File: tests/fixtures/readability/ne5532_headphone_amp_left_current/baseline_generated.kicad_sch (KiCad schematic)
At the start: 13 parts, among them J1 AudioIn_L, J2 AudioIn_R, J3 PowerSupply, J4 HeadphoneOut_L, J5 HeadphoneOut_R

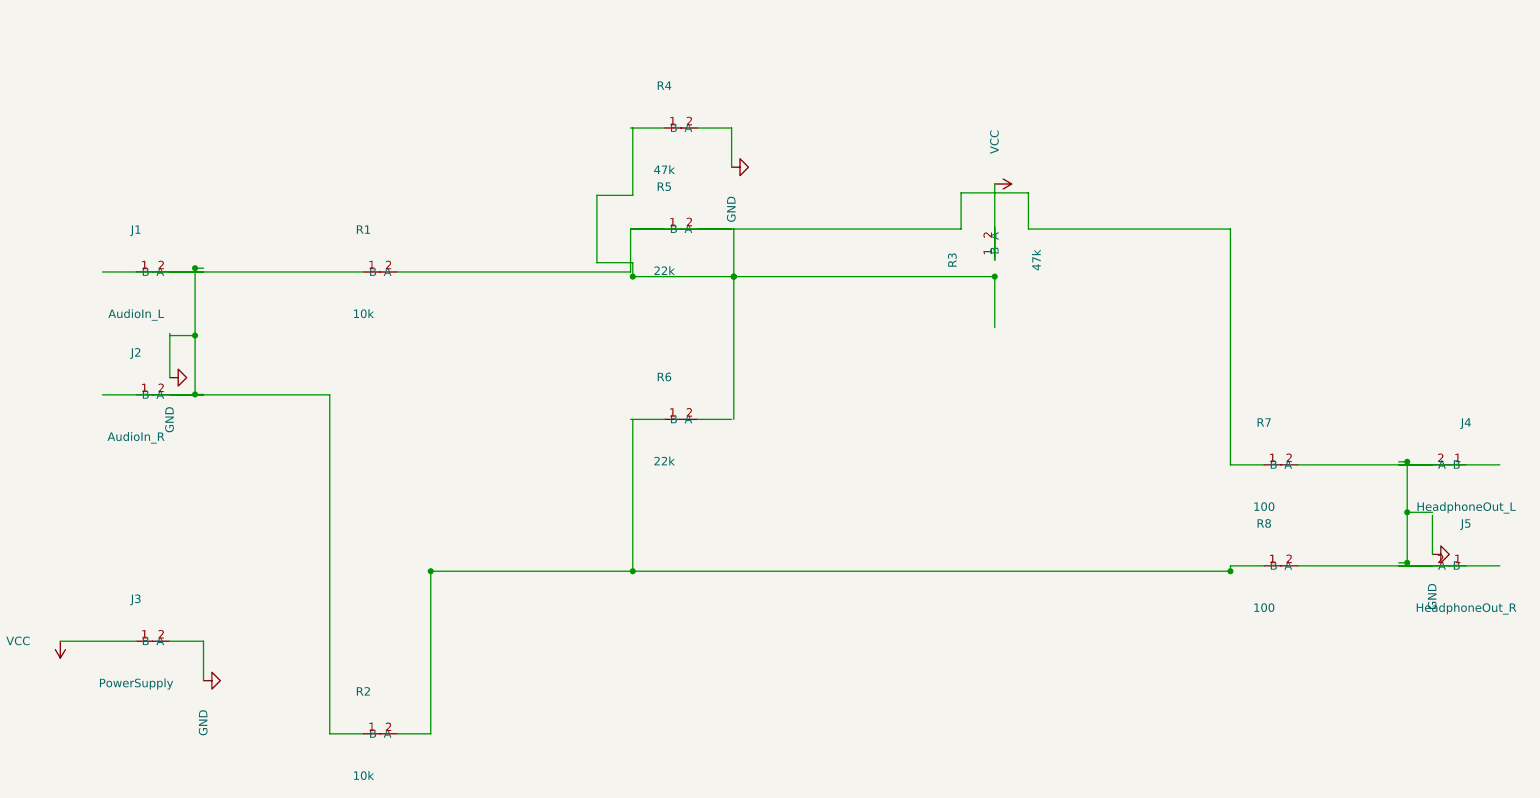
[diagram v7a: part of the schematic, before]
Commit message: feat: improve multi-unit schematic generation
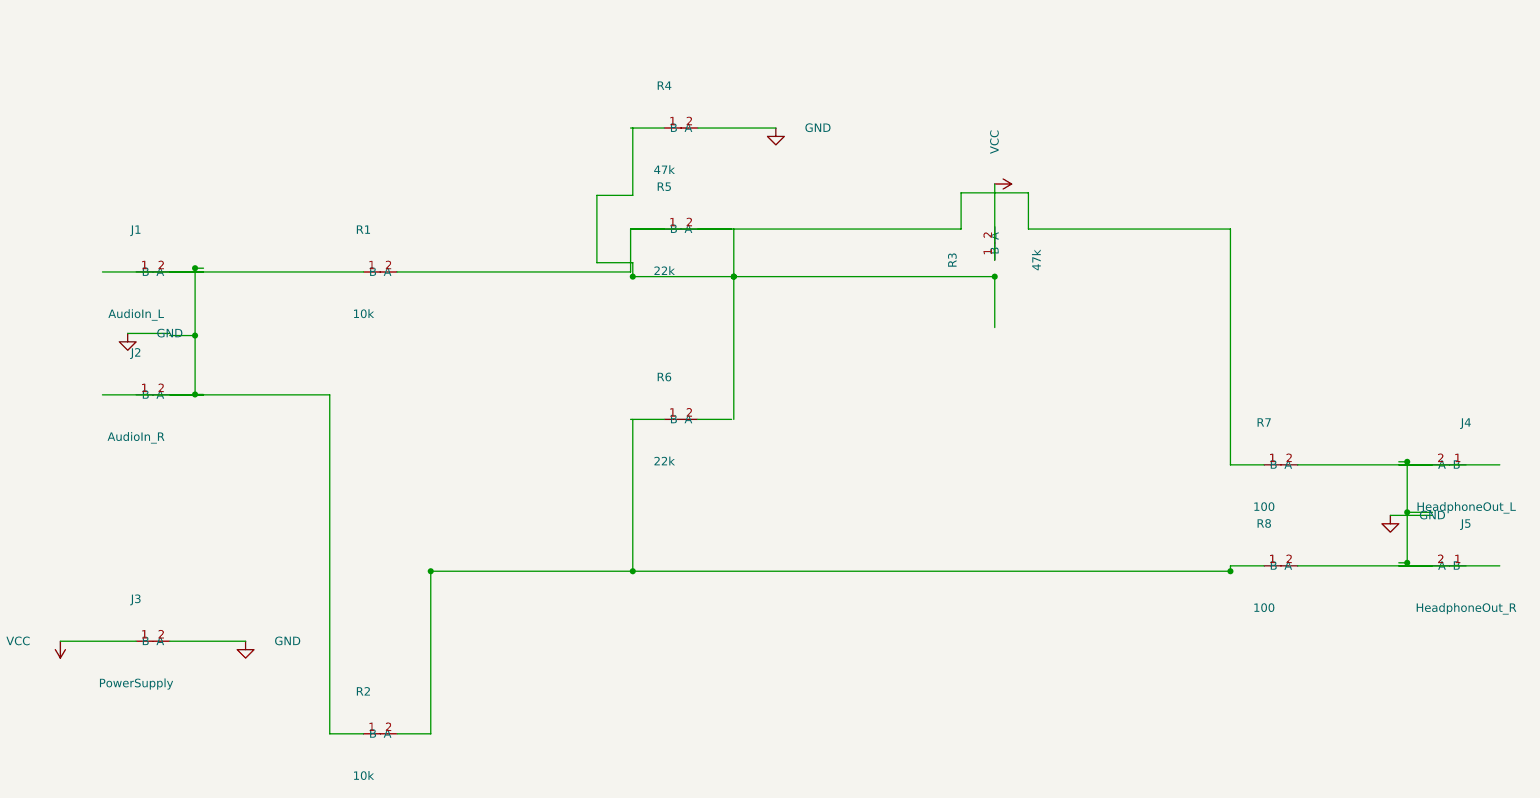
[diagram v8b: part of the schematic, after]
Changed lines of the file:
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@@
         "BaselineHeadphoneAmp"
         (path
-          "/7582036d-d91e-40de-9a75-0636ee5f7de5/"
+          "/32ee968e-6855-4ce4-bd0c-f3703cbcbf44/"
           (reference "J1")
           (unit 1)
@@
         "BaselineHeadphoneAmp"
         (path
-          "/7582036d-d91e-40de-9a75-0636ee5f7de5/"
+          "/32ee968e-6855-4ce4-bd0c-f3703cbcbf44/"
           (reference "J2")
           (unit 1)
@@
         "BaselineHeadphoneAmp"
         (path
-          "/7582036d-d91e-40de-9a75-0636ee5f7de5/"
+          "/32ee968e-6855-4ce4-bd0c-f3703cbcbf44/"
           (reference "J3")
           (unit 1)
@@
         "BaselineHeadphoneAmp"
         (path
-          "/7582036d-d91e-40de-9a75-0636ee5f7de5/"
+          "/32ee968e-6855-4ce4-bd0c-f3703cbcbf44/"
           (reference "J4")
           (unit 1)
@@
         "BaselineHeadphoneAmp"
         (path
-          "/7582036d-d91e-40de-9a75-0636ee5f7de5/"
+          "/32ee968e-6855-4ce4-bd0c-f3703cbcbf44/"
           (reference "J5")
           (unit 1)
@@
         "BaselineHeadphoneAmp"
         (path
-          "/7582036d-d91e-40de-9a75-0636ee5f7de5/"
+          "/32ee968e-6855-4ce4-bd0c-f3703cbcbf44/"
           (reference "R1")
           (unit 1)
@@
         "BaselineHeadphoneAmp"
         (path
-          "/7582036d-d91e-40de-9a75-0636ee5f7de5/"
+          "/32ee968e-6855-4ce4-bd0c-f3703cbcbf44/"
           (reference "R2")
           (unit 1)
@@
         "BaselineHeadphoneAmp"
         (path
-          "/7582036d-d91e-40de-9a75-0636ee5f7de5/"
+          "/32ee968e-6855-4ce4-bd0c-f3703cbcbf44/"
           (reference "R3")
           (unit 1)
@@
         "BaselineHeadphoneAmp"
         (path
-          "/7582036d-d91e-40de-9a75-0636ee5f7de5/"
+          "/32ee968e-6855-4ce4-bd0c-f3703cbcbf44/"
           (reference "R4")
           (unit 1)
@@
         "BaselineHeadphoneAmp"
         (path
-          "/7582036d-d91e-40de-9a75-0636ee5f7de5/"
+          "/32ee968e-6855-4ce4-bd0c-f3703cbcbf44/"
           (reference "R5")
           (unit 1)
@@
         "BaselineHeadphoneAmp"
         (path
-          "/7582036d-d91e-40de-9a75-0636ee5f7de5/"
+          "/32ee968e-6855-4ce4-bd0c-f3703cbcbf44/"
           (reference "R6")
           (unit 1)
@@
         "BaselineHeadphoneAmp"
         (path
-          "/7582036d-d91e-40de-9a75-0636ee5f7de5/"
+          "/32ee968e-6855-4ce4-bd0c-f3703cbcbf44/"
           (reference "R7")
           (unit 1)
@@
         "BaselineHeadphoneAmp"
         (path
-          "/7582036d-d91e-40de-9a75-0636ee5f7de5/"
+          "/32ee968e-6855-4ce4-bd0c-f3703cbcbf44/"
           (reference "R8")
           (unit 1)
@@
   )
   (wire
-    (pts (xy 55.88 108.90) (xy 55.88 115.57))
-    (stroke (width 0) (type default))
-  )
-  (wire
-    (pts (xy 55.88 155.34) (xy 60.96 155.34))
-    (stroke (width 0) (type default))
-  )
-  (wire
-    (pts (xy 60.96 155.34) (xy 60.96 161.29))
+    (pts (xy 55.88 108.90) (xy 49.53 108.90))
+    (stroke (width 0) (type default))
+  )
+  (wire
+    (pts (xy 55.88 155.34) (xy 67.31 155.34))
     (stroke (width 0) (type default))
   )
@@
   )
   (wire
-    (pts (xy 246.38 136.35) (xy 246.38 142.24))
-    (stroke (width 0) (type default))
-  )
-  (wire
-    (pts (xy 135.56 77.91) (xy 140.64 77.91))
-    (stroke (width 0) (type default))
-  )
-  (wire
-    (pts (xy 140.64 77.91) (xy 140.64 83.82))
+    (pts (xy 246.38 136.35) (xy 240.03 136.35))
+    (stroke (width 0) (type default))
+  )
+  (wire
+    (pts (xy 135.56 77.91) (xy 147.32 77.91))
     (stroke (width 0) (type default))
   )
@@
   (symbol
     (lib_id "power:GND")
-    (at 55.88 115.57 90)
+    (at 49.53 108.90 0)
     (unit 1)
     (exclude_from_sim yes)
@@
       "Reference"
       "#PWR01"
-      (at 55.88 115.57 0)
+      (at 49.53 108.90 0)
       (effects (font (size 1.27 1.27)) hide)
     )
@@
       "Value"
       "GND"
-      (at 55.88 121.92 0)
-      (effects (font (size 1.27 1.27)))
-    )
-    (property
-      "Footprint"
-      ""
-      (at 55.88 115.57 0)
-      (effects (font (size 1.27 1.27)) hide)
-    )
-    (property
-      "Datasheet"
-      "~"
-      (at 55.88 115.57 0)
-      (effects (font (size 1.27 1.27)) hide)
-    )
-    (pin "1")
-    (instances
-      (project
-        "BaselineHeadphoneAmp"
-        (path
-          "/7582036d-d91e-40de-9a75-0636ee5f7de5/"
+      (at 55.88 108.90 0)
+      (effects (font (size 1.27 1.27)))
+    )
+    (property
+      "Footprint"
+      ""
+      (at 49.53 108.90 0)
+      (effects (font (size 1.27 1.27)) hide)
+    )
+    (property
+      "Datasheet"
+      "~"
+      (at 49.53 108.90 0)
+      (effects (font (size 1.27 1.27)) hide)
+    )
+    (pin "1")
+    (instances
+      (project
+        "BaselineHeadphoneAmp"
+        (path
+          "/32ee968e-6855-4ce4-bd0c-f3703cbcbf44/"
           (reference "#PWR01")
           (unit 1)
@@
   (symbol
     (lib_id "power:GND")
-    (at 60.96 161.29 90)
+    (at 67.31 155.34 0)
     (unit 1)
     (exclude_from_sim yes)
@@
       "Reference"
       "#PWR02"
-      (at 60.96 161.29 0)
+      (at 67.31 155.34 0)
       (effects (font (size 1.27 1.27)) hide)
     )
@@
       "Value"
       "GND"
-      (at 60.96 167.64 0)
-      (effects (font (size 1.27 1.27)))
-    )
-    (property
-      "Footprint"
-      ""
-      (at 60.96 161.29 0)
-      (effects (font (size 1.27 1.27)) hide)
-    )
-    (property
-      "Datasheet"
-      "~"
-      (at 60.96 161.29 0)
-      (effects (font (size 1.27 1.27)) hide)
-    )
-    (pin "1")
-    (instances
-      (project
-        "BaselineHeadphoneAmp"
-        (path
-          "/7582036d-d91e-40de-9a75-0636ee5f7de5/"
+      (at 73.66 155.34 0)
+      (effects (font (size 1.27 1.27)))
+    )
+    (property
+      "Footprint"
+      ""
+      (at 67.31 155.34 0)
+      (effects (font (size 1.27 1.27)) hide)
+    )
+    (property
+      "Datasheet"
+      "~"
+      (at 67.31 155.34 0)
+      (effects (font (size 1.27 1.27)) hide)
+    )
+    (pin "1")
+    (instances
+      (project
+        "BaselineHeadphoneAmp"
+        (path
+          "/32ee968e-6855-4ce4-bd0c-f3703cbcbf44/"
           (reference "#PWR02")
           (unit 1)
@@
   (symbol
     (lib_id "power:GND")
-    (at 246.38 142.24 90)
+    (at 240.03 136.35 0)
     (unit 1)
     (exclude_from_sim yes)
@@
       "Reference"
       "#PWR03"
-      (at 246.38 142.24 0)
+      (at 240.03 136.35 0)
       (effects (font (size 1.27 1.27)) hide)
     )
@@
       "Value"
       "GND"
-      (at 246.38 148.59 0)
-      (effects (font (size 1.27 1.27)))
-    )
-    (property
-      "Footprint"
-      ""
-      (at 246.38 142.24 0)
-      (effects (font (size 1.27 1.27)) hide)
-    )
-    (property
-      "Datasheet"
-      "~"
-      (at 246.38 142.24 0)
-      (effects (font (size 1.27 1.27)) hide)
-    )
-    (pin "1")
-    (instances
-      (project
-        "BaselineHeadphoneAmp"
-        (path
-          "/7582036d-d91e-40de-9a75-0636ee5f7de5/"
+      (at 246.38 136.35 0)
+      (effects (font (size 1.27 1.27)))
+    )
+    (property
+      "Footprint"
+      ""
+      (at 240.03 136.35 0)
+      (effects (font (size 1.27 1.27)) hide)
+    )
+    (property
+      "Datasheet"
+      "~"
+      (at 240.03 136.35 0)
+      (effects (font (size 1.27 1.27)) hide)
+    )
+    (pin "1")
+    (instances
+      (project
+        "BaselineHeadphoneAmp"
+        (path
+          "/32ee968e-6855-4ce4-bd0c-f3703cbcbf44/"
           (reference "#PWR03")
           (unit 1)
@@
   (symbol
     (lib_id "power:GND")
-    (at 140.64 83.82 90)
+    (at 147.32 77.91 0)
     (unit 1)
     (exclude_from_sim yes)
@@
       "Reference"
       "#PWR04"
-      (at 140.64 83.82 0)
+      (at 147.32 77.91 0)
       (effects (font (size 1.27 1.27)) hide)
     )
@@
       "Value"
       "GND"
-      (at 140.64 90.17 0)
-      (effects (font (size 1.27 1.27)))
-    )
-    (property
-      "Footprint"
-      ""
-      (at 140.64 83.82 0)
-      (effects (font (size 1.27 1.27)) hide)
-    )
-    (property
-      "Datasheet"
-      "~"
-      (at 140.64 83.82 0)
-      (effects (font (size 1.27 1.27)) hide)
-    )
-    (pin "1")
-    (instances
-      (project
-        "BaselineHeadphoneAmp"
-        (path
-          "/7582036d-d91e-40de-9a75-0636ee5f7de5/"
+      (at 153.67 77.91 0)
+      (effects (font (size 1.27 1.27)))
+    )
+    (property
+      "Footprint"
+      ""
+      (at 147.32 77.91 0)
+      (effects (font (size 1.27 1.27)) hide)
+    )
+    (property
+      "Datasheet"
+      "~"
+      (at 147.32 77.91 0)
+      (effects (font (size 1.27 1.27)) hide)
+    )
+    (pin "1")
+    (instances
+      (project
+        "BaselineHeadphoneAmp"
+        (path
+          "/32ee968e-6855-4ce4-bd0c-f3703cbcbf44/"
           (reference "#PWR04")
           (unit 1)
@@
         "BaselineHeadphoneAmp"
         (path
-          "/7582036d-d91e-40de-9a75-0636ee5f7de5/"
+          "/32ee968e-6855-4ce4-bd0c-f3703cbcbf44/"
           (reference "#PWR05")
           (unit 1)
@@
         "BaselineHeadphoneAmp"
         (path
-          "/7582036d-d91e-40de-9a75-0636ee5f7de5/"
+          "/32ee968e-6855-4ce4-bd0c-f3703cbcbf44/"
           (reference "#PWR06")
           (unit 1)
@@
     (effects (font (size 1.27 1.27)) (justify left) hide)
   )
-  (sheet_instances (path "/7582036d-d91e-40de-9a75-0636ee5f7de5/" (page "1")))
+  (sheet_instances (path "/32ee968e-6855-4ce4-bd0c-f3703cbcbf44/" (page "1")))
 )
